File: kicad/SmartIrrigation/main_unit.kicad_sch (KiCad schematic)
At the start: 0 parts

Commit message: Add SDCard class for managing plant data logging and loading
- Created SDCard.cpp and SDCard.h files.
- Implemented methods for loading plant data and logging various plant statuses.
- Prepared the class for future expansion with additional functionalities.
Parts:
- added BAT: Battery_Cell, symbol Device:Battery_Cell
- added ESP: ~, ESP-32, symbol esp32_30pin:ESP32_30Pin
- added IN: Power IN Terminal, symbol Connector:Screw_Terminal_01x02
- added J1, J2, J3, J4, J5, J6, J7, J8: RJ45, Connector_RJ:RJ45_OST_PJ012-8P8CX_Vertical, symbol Connector:RJ45
- added J7: Micro_SD_Card, symbol Connector:Micro_SD_Card
- added LEVEL: ?, Package_DFN_QFN:WQFN-20-1EP_2.5x4.5mm_P0.5mm_EP1x2.9mm, symbol Logic_LevelTranslator:FXMA108
- added MAX: MAX485, Package_SO:SOIC-8_3.9x4.9mm_P1.27mm, symbol Interface_UART:MAX485E
- added PMOS: IRF9540N, Package_TO_SOT_THT:TO-220-3_Vertical, symbol Transistor_FET:IRF9540N
- added R1: 10k, symbol Device:R
- added RTC: DS3231M, Package_SO:SOIC-16W_7.5x10.3mm_P1.27mm, symbol Timer_RTC:DS3231M
- added STEP: TP4057, Package_TO_SOT_SMD:TSOT-23-5, symbol Battery_Management:TP4057
- added TEMP: DHT11, Sensor:Aosong_DHT11_5.5x12.0_P2.54mm, symbol Sensor:DHT11
- added U6: MT3608, Package_TO_SOT_SMD:SOT-23-6, symbol Regulator_Switching:MT3608
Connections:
- new net: BAT.2 (-), STEP.6 (BAT-), U6.4 (EN)
- new net: BAT.1 (+), STEP.3 (BAT), U6.5 (IN)
- new net: IN.1 (Pin_1), STEP.2 (IN-)
- new net: IN.2 (Pin_2), STEP.4 (IN+)
- new net +3.3V: ESP.16 (3.3v), LEVEL.1 (VCCA), RTC.2 (VCC)
- new net A: J1.3, J2.3, J3.3, J4.3, J5.3, J6.3, J7.3, J8.3, MAX.6 (A)
- new net B: J1.4, J2.4, J3.4, J4.4, J5.4, J6.4, J7.4, J8.4, MAX.7 (B)
- new net GND: ESP.2 (GND), J1.5, J1.6, J1.7, J1.8, J2.5, J2.6, J2.7, J2.8, J3.5, J3.6, J3.7, J3.8, J4.5, J4.6, J4.7, J4.8, J5.5, J5.6, J5.7, J5.8, J6.5, J6.6, J6.7, J6.8, J7.1 (GND), J7.5, J7.6, J7.7, J7.8, J8.5, J8.6, J8.7, J8.8, LEVEL.10 (GND), MAX.5 (GND), RTC.10 (GND), RTC.11 (GND), RTC.12 (GND), RTC.13 (GND), RTC.5 (GND), RTC.6 (GND), RTC.7 (GND), RTC.8 (GND), RTC.9 (GND), TEMP.4 (GND), U6.3 (FB)
- new net LEVEL A0 - ESP GPIO16: ESP.21 (GPIO16), LEVEL.3 (A1)
- new net LEVEL A1 - ESP GPIO2: ESP.19 (GPIO2), LEVEL.4 (A2)
- new net LEVEL A4 - ESP GPIO3: ESP.27 (GPIO3), LEVEL.6 (A4)
- new net LEVEL B2 - ESP GPIO17: ESP.22 (GPIO17), LEVEL.5 (A3)
- new net MAX DE/RE - LEVEL B1: MAX.2 (~{RE}), MAX.3 (DE)
- new net MAX DE/RE - LEVEL B2: LEVEL.17 (B2)
- new net MAX DI - LEVEL B2: MAX.4 (DI)
- new net MAX DI - LEVEL B3: LEVEL.16 (B3)
- new net MAX RO - LEVEL B0: MAX.1 (RO)
- new net MAX RO - LEVEL B1: LEVEL.18 (B1)
- new net PMOS GATE - ESP GPIO1: ESP.28 (GPIO1), PMOS.1 (G), R1.2
- new net RTC SCL - ESP GPIO22: ESP.29 (GPIO22), RTC.16 (SCL)
- new net RTC SDA - ESP GPIO21: ESP.26 (GPIO21), RTC.15 (SDA)
- new net RTC SQW - ESP GPIO33: ESP.9 (GPIO33), RTC.3 (~{INT}/SQW)
- new net SD CS - ESP GPIO4: ESP.20 (GPIO4), J7.6 (CS)
- new net SD MISO - ESP GPIO19: ESP.25 (GPIO19), J7.3 (MISO)
- new net SD MOSI - ESP GPIO23: ESP.30 (GPIO23), J7.4 (MOSI)
- new net SD SCK - ESP GPIO18: ESP.24 (GPIO18), J7.5 (SCK)
- new net TEMP DATA - LEVEL B3: TEMP.2 (DATA)
- new net TEMP DATA - LEVEL B4: LEVEL.15 (B4)
- new net VCC_5V: ESP.1 (VIN), PMOS.2 (D), R1.1, U6.1 (SW)
- new net VCC_SWTC: J1.1, J1.2, J2.1, J2.2, J3.1, J3.2, J4.1, J4.2, J5.1, J5.2, J6.1, J6.2, J7.1, J7.2, J7.2 (VCC), J8.1, J8.2, LEVEL.20 (VCCB), MAX.8 (VCC), PMOS.3 (S), TEMP.1 (VDD)

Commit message: new schemes
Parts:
- added D1: 1N5819, Diode_THT:D_DO-41_SOD81_P10.16mm_Horizontal, symbol Diode:1N5819
- added Q1: 2N2222, Package_TO_SOT_THT:TO-39-3, symbol Transistor_BJT:2N2219
- added R2: 1k, symbol Device:R
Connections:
- net MAX DE/RE - LEVEL B1 is gone; now on net MAX DE/RE - LEVEL B2: MAX.2 (~{RE}), MAX.3 (DE)
- net MAX DI - LEVEL B2 is gone; now on net MAX DI - LEVEL B3: MAX.4 (DI)
- net MAX RO - LEVEL B0 is gone; now on net MAX RO - LEVEL B1: MAX.1 (RO)
- net TEMP DATA - LEVEL B3 is gone; now on net TEMP DATA - LEVEL B4: TEMP.2 (DATA)
- net +3.3V: no longer LEVEL.1 (VCCA)
- net GND: now also Q1.1 (E)
- net VCC_5V: now also PMOS.3 (S), R1.2; no longer PMOS.2 (D), R1.1
- net VCC_SWTC: now also PMOS.2 (D); no longer PMOS.3 (S)
- net LEVEL A4 - ESP GPIO5: now reaches ESP.23 (GPIO5)
- net LEVEL A4 - ESP GPIO5: now also LEVEL.6 (A4)
- net SD CS - ESP GPIO12: now reaches ESP.4 (GPIO12)
- net SD CS - ESP GPIO12: now also J7.6 (CS)
- net LEVEL A0 - ESP GPIO16 renamed LEVEL A1 - ESP GPIO16
- net LEVEL A1 - ESP GPIO2 renamed LEVEL A2 - ESP GPIO4
- net LEVEL A2 - ESP GPIO4: now also ESP.20 (GPIO4); no longer ESP.19 (GPIO2)
- net LEVEL A4 - ESP GPIO3: no longer names the net of ESP.27 (GPIO3)
- net LEVEL A4 - ESP GPIO3: no longer LEVEL.6 (A4)
- net LEVEL B2 - ESP GPIO17 renamed LEVEL A3 - ESP GPIO17
- removed net PMOS GATE - ESP GPIO1: ESP.28 (GPIO1), PMOS.1 (G), R1.2
- removed net SD CS - ESP GPIO4: ESP.20 (GPIO4), J7.6 (CS)
- new net: D1.1 (K), LEVEL.1 (VCCA)
- new net: PMOS.1 (G), Q1.3 (C), R1.1
- new net: Q1.2 (B), R2.1
- new net NPN BASE - ESP GPIO2: D1.2 (A), ESP.19 (GPIO2), R2.2
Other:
- moved on the sheet: ESP, MAX, PMOS, R1, TEMP

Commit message: Refactor Controller class and enhance WiFiManager functionality; add sleep feature and improve power management
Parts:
- renumbered Q1 to NPN
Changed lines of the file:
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@@
 		(on_board yes)
 		(dnp no)
-		(property "Reference" "Q1"
+		(property "Reference" "NPN"
 			(at 143.002 72.136 90)
 			(effects
@@
 			(project ""
 				(path "/1fbb681b-0901-4792-bd66-3db0073fd3ce"
-					(reference "Q1")
+					(reference "NPN")
 					(unit 1)
 				)

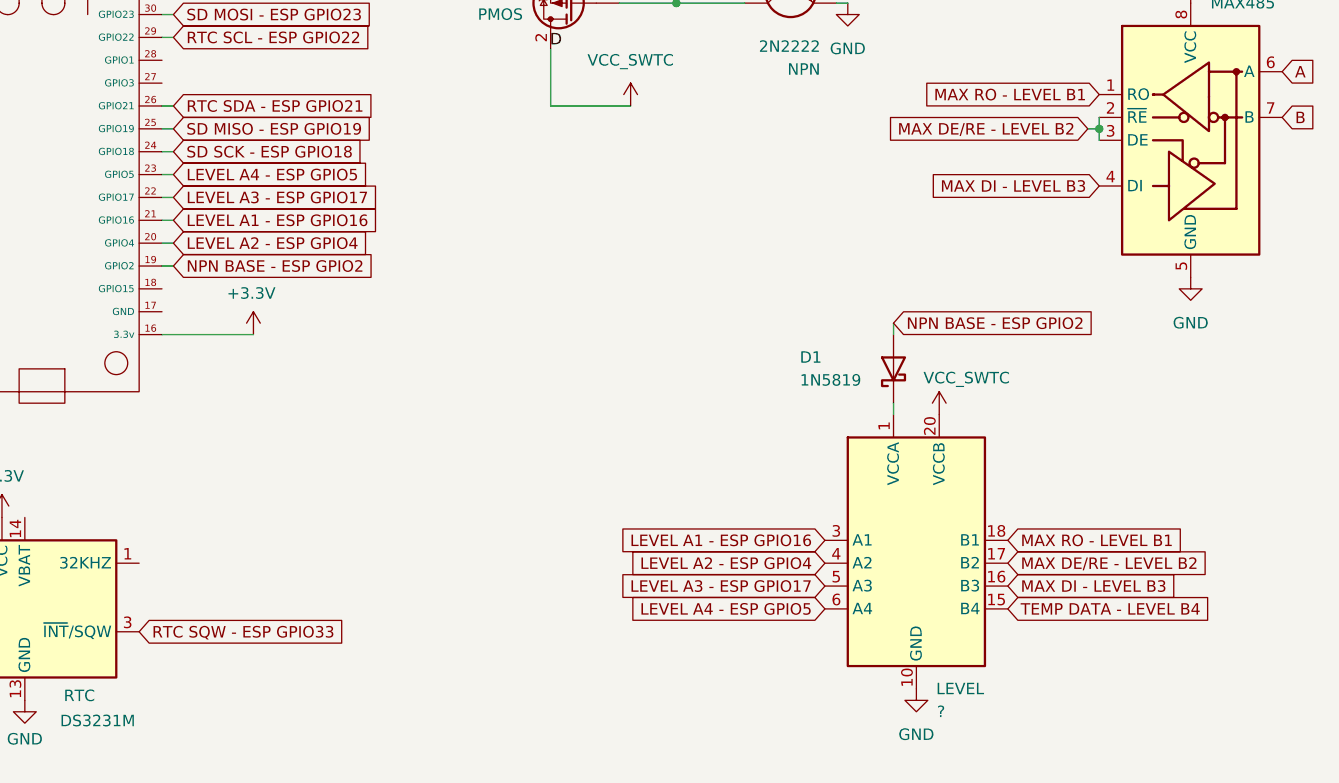
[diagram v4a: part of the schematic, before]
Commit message: updated schematics
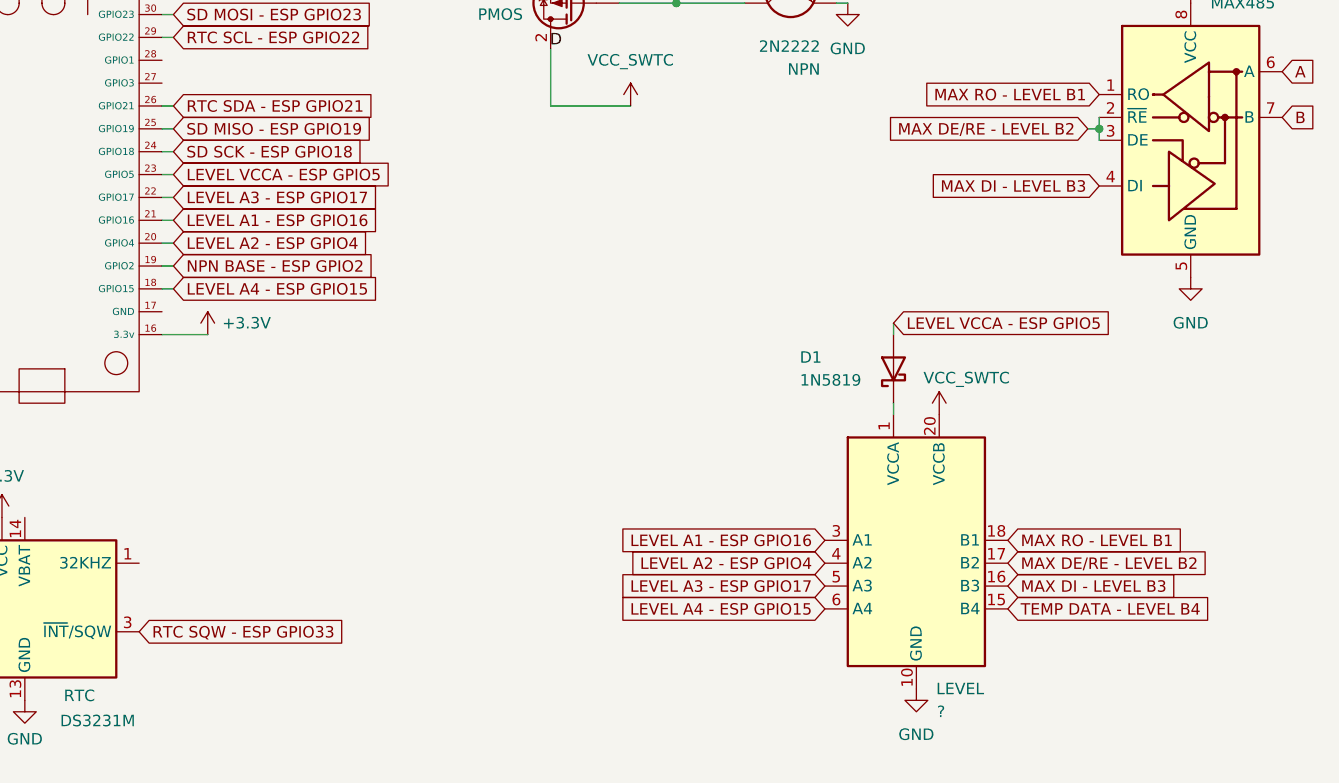
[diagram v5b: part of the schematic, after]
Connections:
- net NPN BASE - ESP GPIO2: no longer D1.2 (A)
- net LEVEL A4 - ESP GPIO15: now reaches ESP.18 (GPIO15)
- net LEVEL A4 - ESP GPIO15: now also LEVEL.6 (A4)
- net LEVEL A4 - ESP GPIO5 renamed LEVEL VCCA - ESP GPIO5
- net LEVEL VCCA - ESP GPIO5: now also D1.2 (A); no longer LEVEL.6 (A4)
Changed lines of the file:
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@@
 	(wire
 		(pts
-			(xy 69.85 101.6) (xy 80.01 101.6)
-		)
-		(stroke
-			(width 0)
-			(type default)
-		)
-	)
-	(wire
-		(pts
-			(xy 69.85 83.82) (xy 71.12 83.82)
+			(xy 69.85 101.6) (xy 74.93 101.6)
 		)
 		(stroke
@@
 	(wire
 		(pts
+			(xy 71.12 83.82) (xy 69.85 83.82)
+		)
+		(stroke
+			(width 0)
+			(type default)
+		)
+	)
+	(wire
+		(pts
 			(xy 212.09 69.85) (xy 215.9 69.85)
 		)
@@
 	(wire
 		(pts
+			(xy 71.12 96.52) (xy 69.85 96.52)
+		)
+		(stroke
+			(width 0)
+			(type default)
+		)
+	)
+	(wire
+		(pts
 			(xy 254 143.51) (xy 254 146.05)
 		)
@@
 		)
 	)
-	(global_label "NPN BASE - ESP GPIO2"
+	(global_label "LEVEL VCCA - ESP GPIO5"
 		(shape input)
 		(at 151.13 100.33 0)
@@
 		)
 		(property "Intersheetrefs" "${INTERSHEET_REFS}"
-			(at 177.5194 100.33 0)
+			(at 179.0313 100.33 0)
 			(effects
 				(font
@@
 		)
 	)
-	(global_label "LEVEL A4 - ESP GPIO5"
+	(global_label "LEVEL A4 - ESP GPIO15"
 		(shape input)
 		(at 143.51 132.08 180)
@@
 		)
 		(property "Intersheetrefs" "${INTERSHEET_REFS}"
-			(at 118.0278 132.08 0)
+			(at 116.8183 132.08 0)
 			(effects
 				(font
@@
 		)
 	)
+	(global_label "LEVEL VCCA - ESP GPIO5"
+		(shape input)
+		(at 71.12 83.82 0)
+		(fields_autoplaced yes)
+		(effects
+			(font
+				(size 1.27 1.27)
+			)
+			(justify left)
+		)
+		(property "Intersheetrefs" "${INTERSHEET_REFS}"
+			(at 99.0213 83.82 0)
+			(effects
+				(font
+					(size 1.27 1.27)
+				)
+				(justify left)
+				(hide yes)
+			)
+		)
+	)
 	(global_label "RTC SQW - ESP GPIO33"
 		(shape input)
@@
 		)
 	)
-	(global_label "LEVEL A4 - ESP GPIO5"
+	(global_label "LEVEL A4 - ESP GPIO15"
 		(shape input)
-		(at 71.12 83.82 0)
+		(at 71.12 96.52 0)
 		(fields_autoplaced yes)
 		(effects
@@
 		)
 		(property "Intersheetrefs" "${INTERSHEET_REFS}"
-			(at 96.6022 83.82 0)
+			(at 97.8117 96.52 0)
 			(effects
 				(font
@@
 	(symbol
 		(lib_id "power:+3.3V")
-		(at 80.01 101.6 0)
+		(at 74.93 101.6 0)
 		(unit 1)
 		(exclude_from_sim no)
@@
 		(dnp no)
 		(property "Reference" "#PWR01"
-			(at 80.01 105.41 0)
+			(at 74.93 105.41 0)
 			(effects
 				(font
@@
 		)
 		(property "Value" "+3.3V"
-			(at 79.756 97.028 0)
+			(at 79.248 100.33 0)
 			(effects
 				(font
@@
 		)
 		(property "Footprint" ""
-			(at 80.01 101.6 0)
+			(at 74.93 101.6 0)
 			(effects
 				(font
@@
 		)
 		(property "Datasheet" ""
-			(at 80.01 101.6 0)
+			(at 74.93 101.6 0)
 			(effects
 				(font
@@
 		)
 		(property "Description" "Power symbol creates a global label with name \"+3.3V\""
-			(at 80.01 101.6 0)
+			(at 74.93 101.6 0)
 			(effects
 				(font

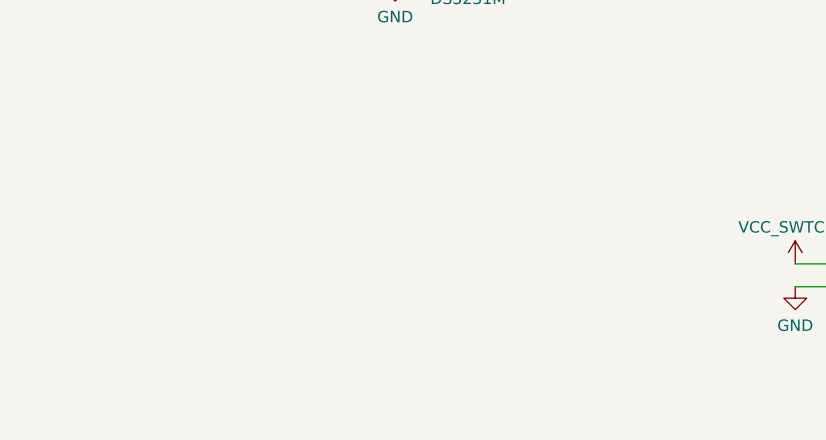
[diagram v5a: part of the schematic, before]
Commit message: Add SD card support
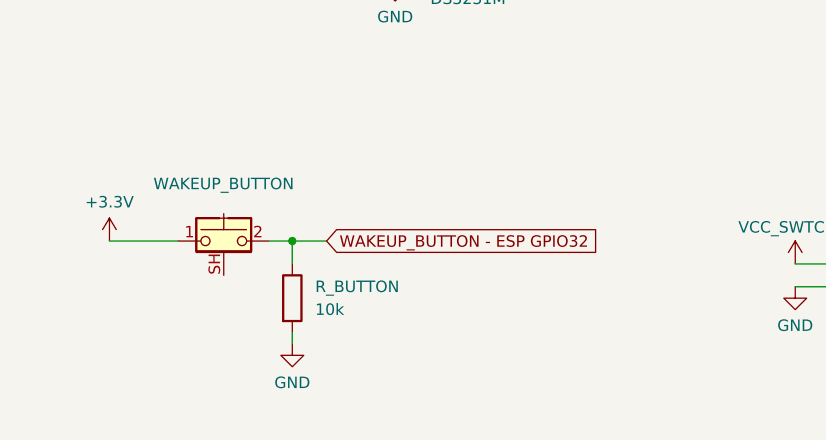
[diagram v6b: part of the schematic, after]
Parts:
- added R_BUTTON: 10k, symbol Device:R
- added WAKEUP_BUTTON: ~, Button_Switch_SMD:SW_SPST_CK_KMS2xxGP, symbol Switch:CK_KMS2xxG
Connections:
- net +3.3V: now also WAKEUP_BUTTON.1
- net GND: now also R_BUTTON.2
- new net WAKEUP_BUTTON - ESP GPIO32: R_BUTTON.1, WAKEUP_BUTTON.2
